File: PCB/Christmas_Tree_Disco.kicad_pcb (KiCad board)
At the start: 2 copper layers, 190.5 x 188.9 mm, 136 parts, among them J1 PJ-006B-SMT-TR, U1 DEV_KIT_EK-TM4C123GXL, U2 TLC5955DCA, U3 LM1085-5.0

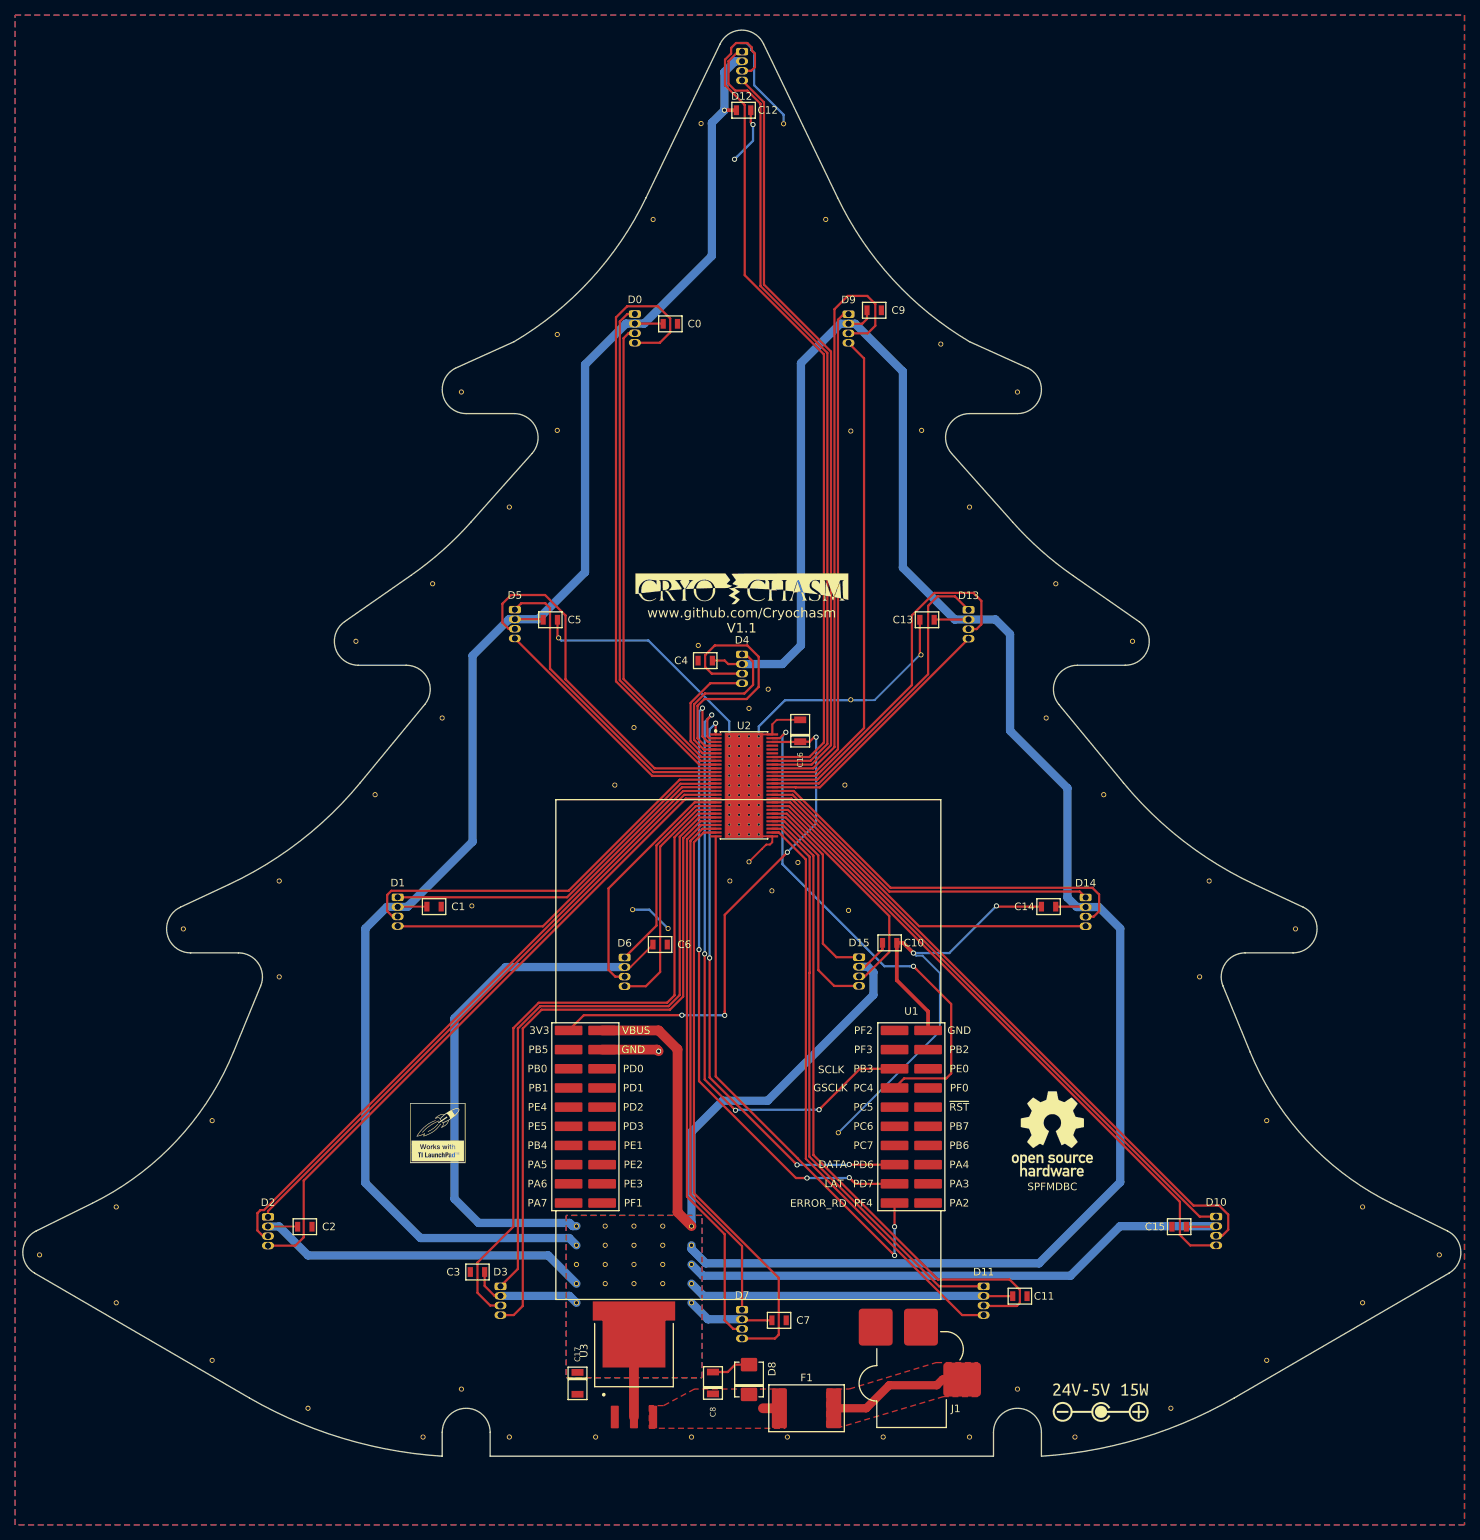
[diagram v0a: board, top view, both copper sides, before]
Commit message: Schematic V2
REQUIRES CHANGE TO SOFTWARE: Changed pin of LAT from D7 to D0 to avoid
using the non-maskable interrupt pin.

Added a SMD LED D8 to provide and enviornmental lighting effect.

Removed power supply circuit; USB power from the dev board is sufficent
for
LED brightness. Must be plugged into USB 3.0 or a 2A rated supply.

Updated symbol library to use KiBOM and to Lib Version 4.

TODO: Update  PCB
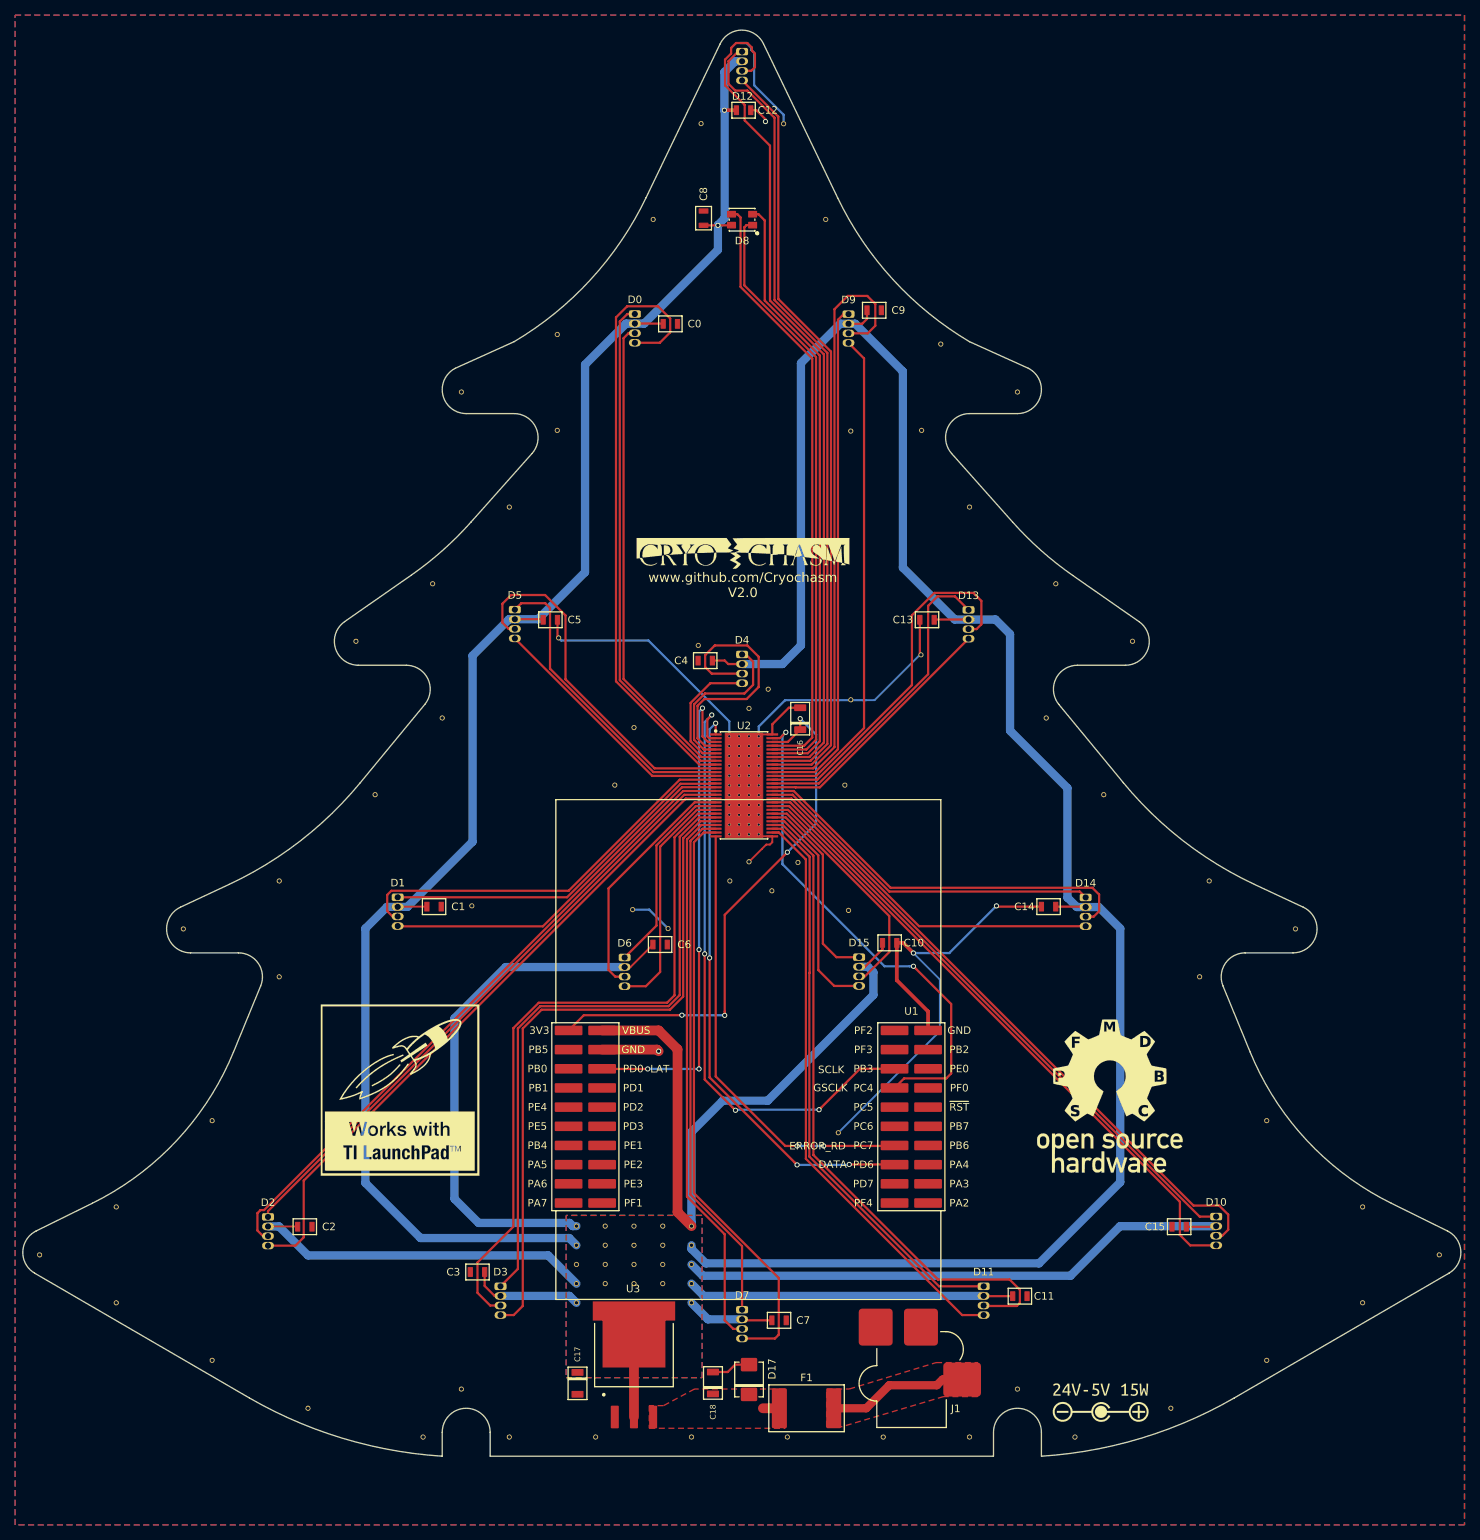
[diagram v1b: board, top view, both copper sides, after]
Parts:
- removed V1.1: www.github.com/Cryochasm, local:Cryochasm
- added C8: 0.1u, local:SMD-0805, F.Cu at (103.2, 51.9)
- added D8: AAA3528SEEZGKQBKS, local:PLCC-4-3.5x2.8, F.Cu at (108.3, 52.1)
- added V2.0: www.github.com/Cryochasm, local:Cryochasm, F.Cu at (108.4, 96.3)
- D0, D1, D10, D11, D12, D13, D14, D15, D2, D3, D4, D5, D6, D7, D9: moved to B.Cu
- moved H7 9.10 mm to (157.0, 168.2)
- moved H1 7.58 mm to (63.0, 167.4)
- moved C16 1.60 mm to (116.0, 118.2)
- turned D0 to 180 degrees
- turned D1 to 180 degrees
- turned D10 to 180 degrees
- turned D11 to 180 degrees
- turned D12 to 180 degrees
- turned D13 to 180 degrees
- turned D14 to 180 degrees
- turned D15 to 180 degrees
- turned D2 to 180 degrees
- turned D3 to 180 degrees
- turned D4 to 180 degrees
- turned D5 to 180 degrees
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- renumbered C8 to C18, D8 to D17
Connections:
- J1 pad 3: (no net) -> Net-(J1-Pad3)
- U1 pad 10: (no net) -> Net-(U1-Pad10)
- U1 pad 11: (no net) -> Net-(U1-Pad11)
- U1 pad 12: (no net) -> Net-(U1-Pad12)
- U1 pad 13: (no net) -> Net-(U1-Pad13)
- U1 pad 14: (no net) -> Net-(U1-Pad14)
- U1 pad 15: (no net) -> Net-(U1-Pad15)
- U1 pad 16: (no net) -> Net-(U1-Pad16)
- U1 pad 17: (no net) -> Net-(U1-Pad17)
- U1 pad 18: (no net) -> /Top Sheet/Microcontroller/LAT
- U1 pad 2: (no net) -> Net-(U1-Pad2)
- U1 pad 21: (no net) -> Net-(U1-Pad21)
- U1 pad 22: (no net) -> Net-(U1-Pad22)
- U1 pad 25: Net-(U1-Pad25) -> (no net)
- U1 pad 26: (no net) -> Net-(U1-Pad26)
- U1 pad 27: Net-(U1-Pad27) -> /Top Sheet/Microcontroller/ERROR_RD
- U1 pad 29: /Top Sheet/Microcontroller/LAT -> Net-(U1-Pad29)
- U1 pad 3: (no net) -> Net-(U1-Pad3)
- U1 pad 30: /Top Sheet/Microcontroller/ERROR_RD -> Net-(U1-Pad30)
- U1 pad 31: (no net) -> Net-(U1-Pad31)
- U1 pad 32: (no net) -> Net-(U1-Pad32)
- U1 pad 33: (no net) -> Net-(U1-Pad33)
- U1 pad 34: (no net) -> Net-(U1-Pad34)
- U1 pad 35: (no net) -> Net-(U1-Pad35)
- U1 pad 36: (no net) -> Net-(U1-Pad36)
- U1 pad 37: (no net) -> Net-(U1-Pad37)
- U1 pad 38: (no net) -> Net-(U1-Pad38)
- U1 pad 39: (no net) -> Net-(U1-Pad39)
- U1 pad 4: (no net) -> Net-(U1-Pad4)
- U1 pad 5: (no net) -> Net-(U1-Pad5)
- U1 pad 6: (no net) -> Net-(U1-Pad6)
- U1 pad 7: (no net) -> Net-(U1-Pad7)
- U1 pad 8: (no net) -> Net-(U1-Pad8)
- U1 pad 9: (no net) -> Net-(U1-Pad9)
- U2 pad 51: (no net) -> Net-(D8-Pad3)
- U2 pad 52: (no net) -> Net-(D8-Pad1)
- U2 pad 53: (no net) -> Net-(D8-Pad4)
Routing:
- net Net-(D8-Pad3): track 0.00 -> 80.9 mm
- net Net-(D8-Pad4): track 0.00 -> 80.0 mm
- net Net-(D8-Pad1): track 0.00 -> 79.4 mm
- net /Top Sheet/Microcontroller/LAT: track 87.0 -> 66.6 mm
- net /Top Sheet/Microcontroller/ERROR_RD: track 72.3 -> 59.3 mm
- net /Top Sheet/Microcontroller/GND: track 185.1 -> 180.4 mm, vias 5 -> 4
- net /Top Sheet/Microcontroller/5V: track 852.8 -> 856.5 mm, vias 1 -> 2
- net /Top Sheet/Microcontroller/3V3: track 69.5 -> 72.5 mm
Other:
- net class Default: clearance 0.16 -> 0
- rule trace_clearance: 0.16 -> 0
